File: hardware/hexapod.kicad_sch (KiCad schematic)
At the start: 69 parts, among them J1 Conn_01x01_Pin, J10 Conn_01x01_Pin, J10_L_{3}_COXA1 Conn_01x03_Pin, J11 Conn_01x01_Pin, J11_L_{4}_COXA1 Conn_01x03_Pin, J12 Conn_01x01_Pin, J12_L_{3}_FEMUR1 Conn_01x03_Pin, J13 Conn_01x01_Pin, J13_L_{4}_FEMUR1 Conn_01x03_Pin, J14 Conn_01x01_Pin, J14_L_{3}_TIBIA1 Conn_01x03_Pin, J15 Conn_01x01_Pin, J15_L_{4}_TIBIA1 Conn_01x03_Pin, J16 Conn_01x01_Pin, J16_L_{5}_COXA1 Conn_01x03_Pin, J17 Conn_01x01_Pin, J17_L_{6}_COXA1 Conn_01x03_Pin, J18 Conn_01x01_Pin, J18_L_{5}_FEMUR1 Conn_01x03_Pin, J19 Conn_01x01_Pin, J19_L_{6}_FEMUR1 Conn_01x03_Pin, J1_L_{1}_COXA1 Conn_01x03_Pin, J2 Barrel_Jack, J20 Conn_01x01_Pin, J20_L_{5}_TIBIA1 Conn_01x03_Pin, J21 Conn_01x01_Pin, J21_L_{6}_TIBIA1 Conn_01x03_Pin, J22 Barrel_Jack, J23 Reveiver, J3 Barrel_Jack, J4 Barrel_Jack, J5 Conn_01x01_Pin, J5_L_{1}_FEMUR1 Conn_01x03_Pin, J6 Conn_01x01_Pin, J6_L_{1}_TIBIA1 Conn_01x03_Pin, J7 Conn_01x01_Pin, J7_L_{2}_COXA1 Conn_01x03_Pin, J8 Conn_01x01_Pin, J8_L_{2}_FEMUR1 Conn_01x03_Pin, J9 Conn_01x01_Pin, J9_L_{2}_TIBIA1 Conn_01x03_Pin, U1 ESP32-WROOM-32D

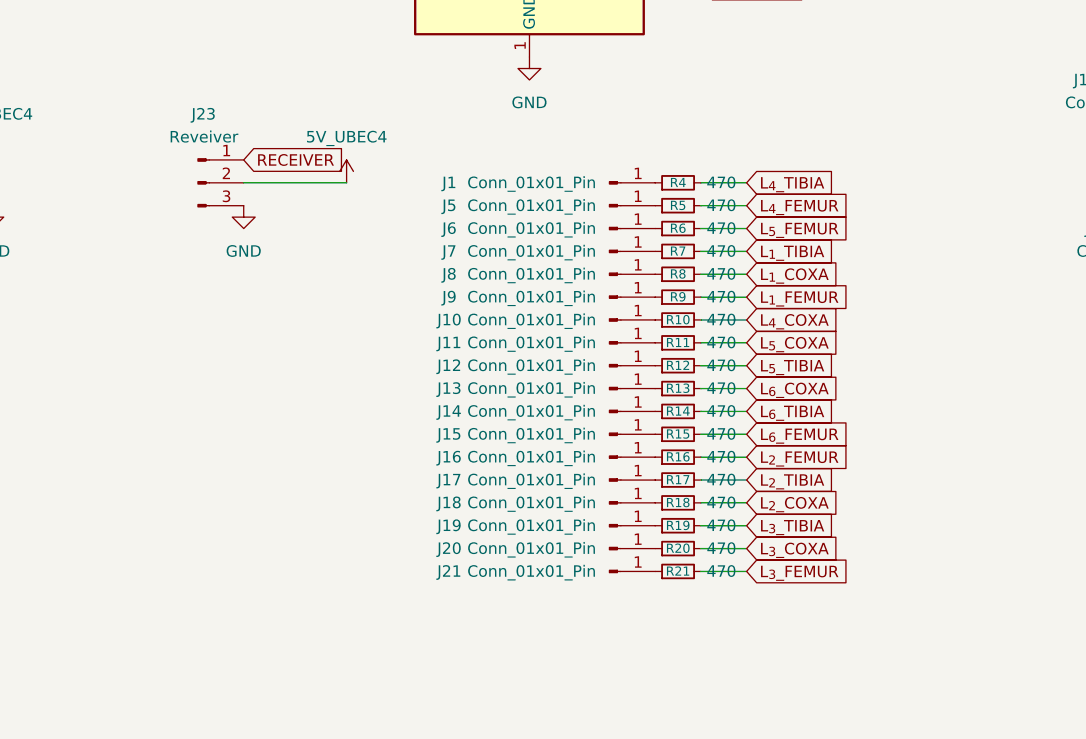
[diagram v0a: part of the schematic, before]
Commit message: add FFC connector
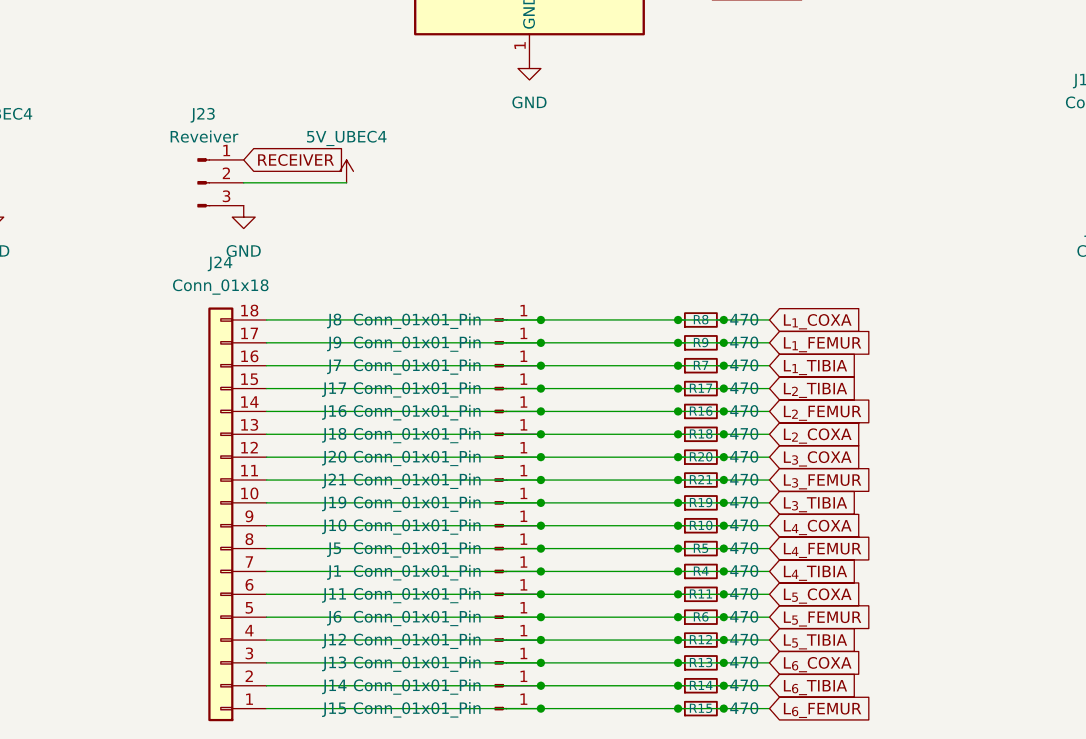
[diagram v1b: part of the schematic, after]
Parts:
- added J24: Conn_01x18, Connector_FFC-FPC:TE_1-84952-8_1x18-1MP_P1.0mm_Horizontal, symbol Connector_Generic:Conn_01x18
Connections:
- net L_{1}_COXA: now also J8.1 (Pin_1), R8.1, J24.18 (Pin_18)
- net L_{1}_FEMUR: now also J9.1 (Pin_1), R9.1, J24.17 (Pin_17)
- net L_{1}_TIBIA: now also J7.1 (Pin_1), R7.1, J24.16 (Pin_16)
- net L_{2}_COXA: now also J18.1 (Pin_1), R18.1, J24.13 (Pin_13)
- net L_{2}_FEMUR: now also J16.1 (Pin_1), R16.1, J24.14 (Pin_14)
- net L_{2}_TIBIA: now also J17.1 (Pin_1), R17.1, J24.15 (Pin_15)
- net L_{3}_COXA: now also J20.1 (Pin_1), R20.1, J24.12 (Pin_12)
- net L_{3}_FEMUR: now also J21.1 (Pin_1), R21.1, J24.11 (Pin_11)
- net L_{3}_TIBIA: now also J19.1 (Pin_1), R19.1, J24.10 (Pin_10)
- net L_{4}_COXA: now also J10.1 (Pin_1), R10.1, J24.9 (Pin_9)
- net L_{4}_FEMUR: now also J5.1 (Pin_1), R5.1, J24.8 (Pin_8)
- net L_{4}_TIBIA: now also J1.1 (Pin_1), R4.1, J24.7 (Pin_7)
- net L_{5}_COXA: now also J11.1 (Pin_1), R11.1, J24.6 (Pin_6)
- net L_{5}_FEMUR: now also J6.1 (Pin_1), R6.1, J24.5 (Pin_5)
- net L_{5}_TIBIA: now also J12.1 (Pin_1), R12.1, J24.4 (Pin_4)
- net L_{6}_COXA: now also J13.1 (Pin_1), R13.1, J24.3 (Pin_3)
- net L_{6}_FEMUR: now also J15.1 (Pin_1), R15.1, J24.1 (Pin_1)
- net L_{6}_TIBIA: now also J14.1 (Pin_1), R14.1, J24.2 (Pin_2)
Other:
- moved on the sheet: J1, J10, J11, J12, J13, J14, J15, J16, J17, J18, J19, J20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
